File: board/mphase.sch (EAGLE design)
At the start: 4 parts, among them IC1 MAX232, IC2 PIC18F4455_40, X1 332-10, X2 332-10

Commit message: updates
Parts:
- added C1, C2, C3, C4, C5, C6, C7: (no value), resistor:C-US025-025X050
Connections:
- new net N$1: C1.2, IC1G$1.C1-
- new net N$10: IC1G$1.T2IN, IC2.TX2
- new net N$11: IC1G$1.T1IN, IC2.TX1
- new net N$12: IC1G$1.R1OUT, IC2.RX1
- new net N$13: IC1G$1.R2OUT, IC2.RX2
- new net N$2: C2.2, IC1G$1.C2-
- new net N$3: C2.1, IC1G$1.C2+
- new net N$4: C1.1, IC1G$1.C1+
- new net N$5: C3.2, IC1G$1.V+
- new net N$6: C4.1, IC1G$1.V-
- new net N$9: C5.1, IC2.VDDCORE
- new net VDD: C6.1, C7.1, IC2.VDD, IC2.VDD@1
- new net VSS: C3.1, C4.2, C7.2, IC2.VSS, IC2.VSS@1
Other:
- moved on the sheet: IC1, IC2
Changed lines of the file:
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@@
 <layer number="97" name="Info" color="7" fill="1" visible="yes" active="yes"/>
 <layer number="98" name="Guide" color="6" fill="1" visible="yes" active="yes"/>
+<layer number="99" name="SpiceOrder" color="5" fill="1" visible="yes" active="yes"/>
 </layers>
 <schematic xreflabel="%F%N/%S.%C%R" xrefpart="/%S.%C%R">
@@
 <part name="X2" library="con-garry" deviceset="332-10" device=""/>
 <part name="IC2" library="microchip" deviceset="PIC18F4*_40" device="" technology="455"/>
+<part name="C1" library="resistor" deviceset="C-US" device="025-025X050"/>
+<part name="C2" library="resistor" deviceset="C-US" device="025-025X050"/>
+<part name="C3" library="resistor" deviceset="C-US" device="025-025X050"/>
+<part name="C4" library="resistor" deviceset="C-US" device="025-025X050"/>
+<part name="C5" library="resistor" deviceset="C-US" device="025-025X050"/>
+<part name="C6" library="resistor" deviceset="C-US" device="025-025X050"/>
+<part name="C7" library="resistor" deviceset="C-US" device="025-025X050"/>
+<part name="VDD1" library="supply1" deviceset="VDD" device=""/>
+<part name="VDD2" library="supply1" deviceset="VDD" device=""/>
+<part name="VSS1" library="supply1" deviceset="VSS" device=""/>
+<part name="VSS2" library="supply1" deviceset="VSS" device=""/>
+<part name="VSS3" library="supply1" deviceset="VSS" device=""/>
+<part name="VSS4" library="supply1" deviceset="VSS" device=""/>
+<part name="VSS5" library="supply1" deviceset="VSS" device=""/>
+<part name="VSS6" library="supply1" deviceset="VSS" device=""/>
+<part name="VSS7" library="supply1" deviceset="VSS" device=""/>
 </parts>
 <sheets>
@@
 </plain>
 <instances>
-<instance part="IC1" gate="G$1" x="33.02" y="43.18"/>
+<instance part="IC1" gate="G$1" x="152.4" y="48.26"/>
 <instance part="X1" gate="-1" x="25.4" y="99.06"/>
 <instance part="X1" gate="-2" x="45.72" y="99.06"/>
@@
 <instance part="X2" gate="-9" x="91.44" y="88.9"/>
 <instance part="X2" gate="-10" x="111.76" y="88.9"/>
-<instance part="IC2" gate="G$1" x="93.98" y="45.72"/>
+<instance part="IC2" gate="G$1" x="40.64" y="45.72"/>
+<instance part="C1" gate="G$1" x="129.54" y="60.96"/>
+<instance part="C2" gate="G$1" x="129.54" y="50.8"/>
+<instance part="C3" gate="G$1" x="172.72" y="63.5"/>
+<instance part="C4" gate="G$1" x="177.8" y="50.8"/>
+<instance part="C5" gate="G$1" x="-10.16" y="58.42" rot="R270"/>
+<instance part="C6" gate="G$1" x="-10.16" y="45.72" rot="R270"/>
+<instance part="C7" gate="G$1" x="86.36" y="50.8" rot="R90"/>
+<instance part="VDD1" gate="G$1" x="-5.08" y="48.26"/>
+<instance part="VDD2" gate="G$1" x="83.82" y="53.34"/>
+<instance part="VSS1" gate="G$1" x="78.74" y="48.26" rot="R90"/>
+<instance part="VSS2" gate="G$1" x="177.8" y="43.18"/>
+<instance part="VSS3" gate="G$1" x="172.72" y="68.58" rot="R180"/>
+<instance part="VSS4" gate="G$1" x="93.98" y="50.8" rot="R90"/>
+<instance part="VSS5" gate="G$1" x="-15.24" y="45.72" rot="R270"/>
+<instance part="VSS6" gate="G$1" x="-15.24" y="58.42" rot="R270"/>
+<instance part="VSS7" gate="G$1" x="2.54" y="43.18" rot="R270"/>
 </instances>
 <busses>
 </busses>
 <nets>
+<net name="N$1" class="0">
+<segment>
+<pinref part="C1" gate="G$1" pin="2"/>
+<pinref part="IC1" gate="G$1" pin="C1-"/>
+<wire x1="129.54" y1="55.88" x2="137.16" y2="55.88" width="0.1524" layer="91"/>
+</segment>
+</net>
+<net name="N$2" class="0">
+<segment>
+<pinref part="C2" gate="G$1" pin="2"/>
+<pinref part="IC1" gate="G$1" pin="C2-"/>
+<wire x1="129.54" y1="45.72" x2="137.16" y2="45.72" width="0.1524" layer="91"/>
+</segment>
+</net>
+<net name="N$3" class="0">
+<segment>
+<pinref part="C2" gate="G$1" pin="1"/>
+<wire x1="129.54" y1="53.34" x2="137.16" y2="53.34" width="0.1524" layer="91"/>
+<pinref part="IC1" gate="G$1" pin="C2+"/>
+<wire x1="137.16" y1="53.34" x2="137.16" y2="50.8" width="0.1524" layer="91"/>
+</segment>
+</net>
+<net name="N$4" class="0">
+<segment>
+<pinref part="C1" gate="G$1" pin="1"/>
+<wire x1="129.54" y1="63.5" x2="137.16" y2="63.5" width="0.1524" layer="91"/>
+<pinref part="IC1" gate="G$1" pin="C1+"/>
+<wire x1="137.16" y1="63.5" x2="137.16" y2="60.96" width="0.1524" layer="91"/>
+</segment>
+</net>
+<net name="N$5" class="0">
+<segment>
+<pinref part="IC1" gate="G$1" pin="V+"/>
+<pinref part="C3" gate="G$1" pin="2"/>
+<wire x1="167.64" y1="58.42" x2="172.72" y2="58.42" width="0.1524" layer="91"/>
+</segment>
+</net>
+<net name="N$6" class="0">
+<segment>
+<pinref part="IC1" gate="G$1" pin="V-"/>
+<pinref part="C4" gate="G$1" pin="1"/>
+<wire x1="167.64" y1="53.34" x2="177.8" y2="53.34" width="0.1524" layer="91"/>
+</segment>
+</net>
+<net name="N$9" class="0">
+<segment>
+<pinref part="IC2" gate="G$1" pin="VDDCORE"/>
+<pinref part="C5" gate="G$1" pin="1"/>
+<wire x1="5.08" y1="58.42" x2="-7.62" y2="58.42" width="0.1524" layer="91"/>
+</segment>
+</net>
+<net name="N$10" class="0">
+<segment>
+<pinref part="IC2" gate="G$1" pin="TX2"/>
+<wire x1="76.2" y1="43.18" x2="104.14" y2="43.18" width="0.1524" layer="91"/>
+<wire x1="104.14" y1="43.18" x2="104.14" y2="38.1" width="0.1524" layer="91"/>
+<pinref part="IC1" gate="G$1" pin="T2IN"/>
+<wire x1="104.14" y1="38.1" x2="137.16" y2="38.1" width="0.1524" layer="91"/>
+</segment>
+</net>
+<net name="N$11" class="0">
+<segment>
+<pinref part="IC2" gate="G$1" pin="TX1"/>
+<wire x1="76.2" y1="33.02" x2="106.68" y2="33.02" width="0.1524" layer="91"/>
+<wire x1="106.68" y1="33.02" x2="106.68" y2="40.64" width="0.1524" layer="91"/>
+<pinref part="IC1" gate="G$1" pin="T1IN"/>
+<wire x1="106.68" y1="40.64" x2="137.16" y2="40.64" width="0.1524" layer="91"/>
+</segment>
+</net>
+<net name="N$12" class="0">
+<segment>
+<pinref part="IC2" gate="G$1" pin="RX1"/>
+<pinref part="IC1" gate="G$1" pin="R1OUT"/>
+<wire x1="76.2" y1="35.56" x2="137.16" y2="35.56" width="0.1524" layer="91"/>
+</segment>
+</net>
+<net name="N$13" class="0">
+<segment>
+<pinref part="IC2" gate="G$1" pin="RX2"/>
+<wire x1="76.2" y1="45.72" x2="109.22" y2="45.72" width="0.1524" layer="91"/>
+<wire x1="109.22" y1="45.72" x2="109.22" y2="33.02" width="0.1524" layer="91"/>
+<pinref part="IC1" gate="G$1" pin="R2OUT"/>
+<wire x1="109.22" y1="33.02" x2="137.16" y2="33.02" width="0.1524" layer="91"/>
+</segment>
+</net>
+<net name="VDD" class="0">
+<segment>
+<pinref part="C6" gate="G$1" pin="1"/>
+<pinref part="IC2" gate="G$1" pin="VDD"/>
+<wire x1="-7.62" y1="45.72" x2="-5.08" y2="45.72" width="0.1524" layer="91"/>
+<pinref part="VDD1" gate="G$1" pin="VDD"/>
+<wire x1="-5.08" y1="45.72" x2="5.08" y2="45.72" width="0.1524" layer="91"/>
+<junction x="-5.08" y="45.72"/>
+</segment>
+<segment>
+<pinref part="C7" gate="G$1" pin="1"/>
+<pinref part="IC2" gate="G$1" pin="VDD@1"/>
+<wire x1="83.82" y1="50.8" x2="76.2" y2="50.8" width="0.1524" layer="91"/>
+<pinref part="VDD2" gate="G$1" pin="VDD"/>
+<junction x="83.82" y="50.8"/>
+</segment>
+</net>
+<net name="VSS" class="0">
+<segment>
+<pinref part="C4" gate="G$1" pin="2"/>
+<pinref part="VSS2" gate="G$1" pin="VSS"/>
+</segment>
+<segment>
+<pinref part="C3" gate="G$1" pin="1"/>
+<pinref part="VSS3" gate="G$1" pin="VSS"/>
+</segment>
+<segment>
+<pinref part="C7" gate="G$1" pin="2"/>
+<pinref part="VSS4" gate="G$1" pin="VSS"/>
+</segment>
+<segment>
+<pinref part="IC2" gate="G$1" pin="VSS"/>
+<pinref part="VSS7" gate="G$1" pin="VSS"/>
+</segment>
+<segment>
+<pinref part="IC2" gate="G$1" pin="VSS@1"/>
+<pinref part="VSS1" gate="G$1" pin="VSS"/>
+</segment>
+</net>
 </nets>
 </sheet>

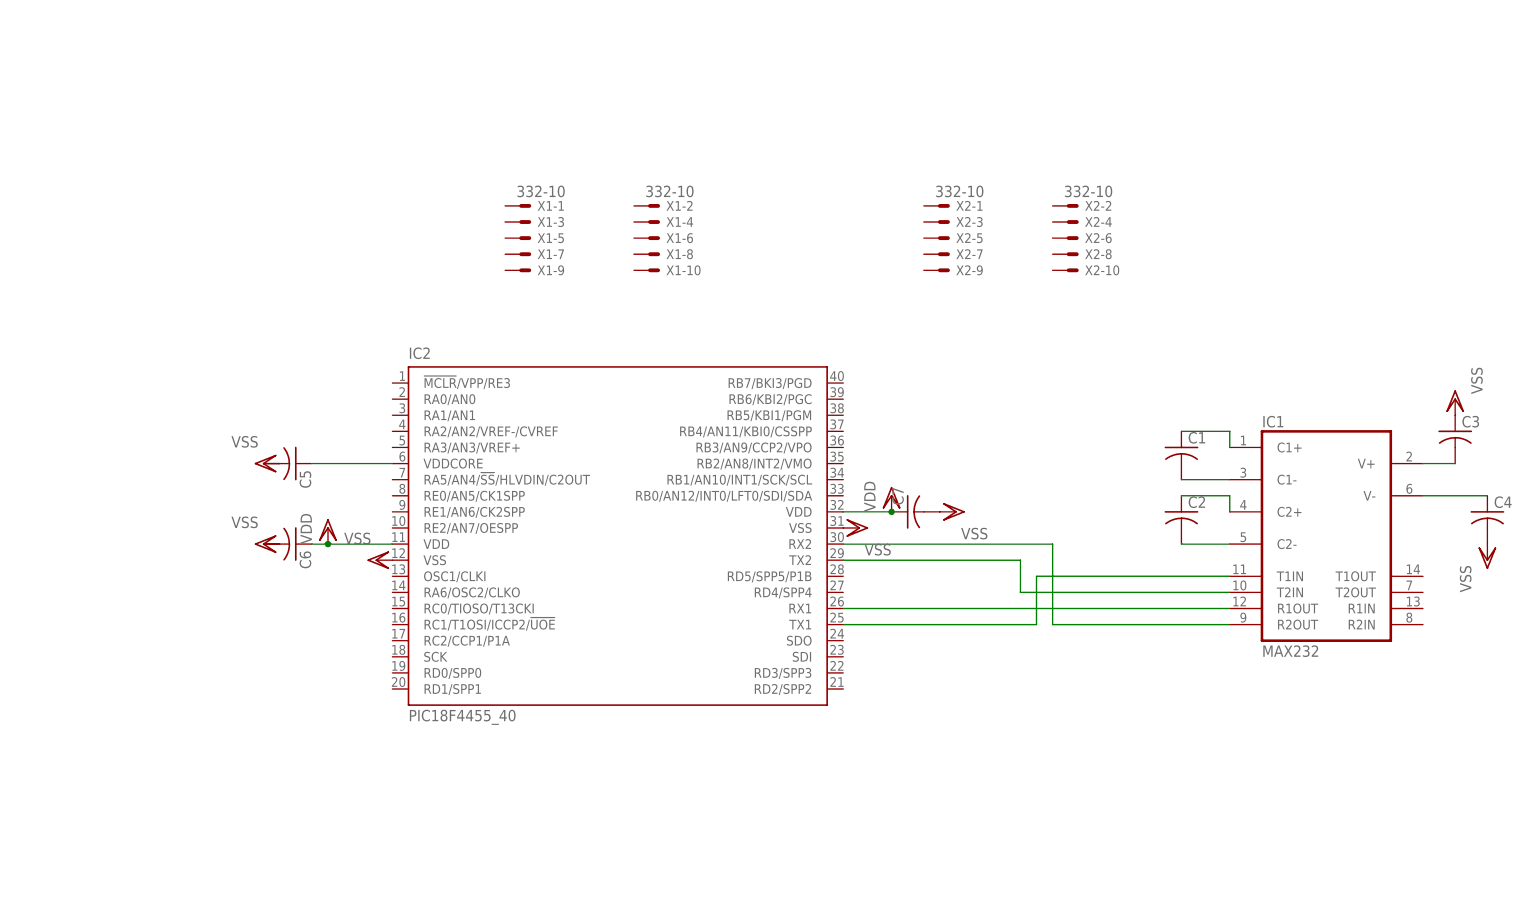
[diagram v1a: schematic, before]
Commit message: 
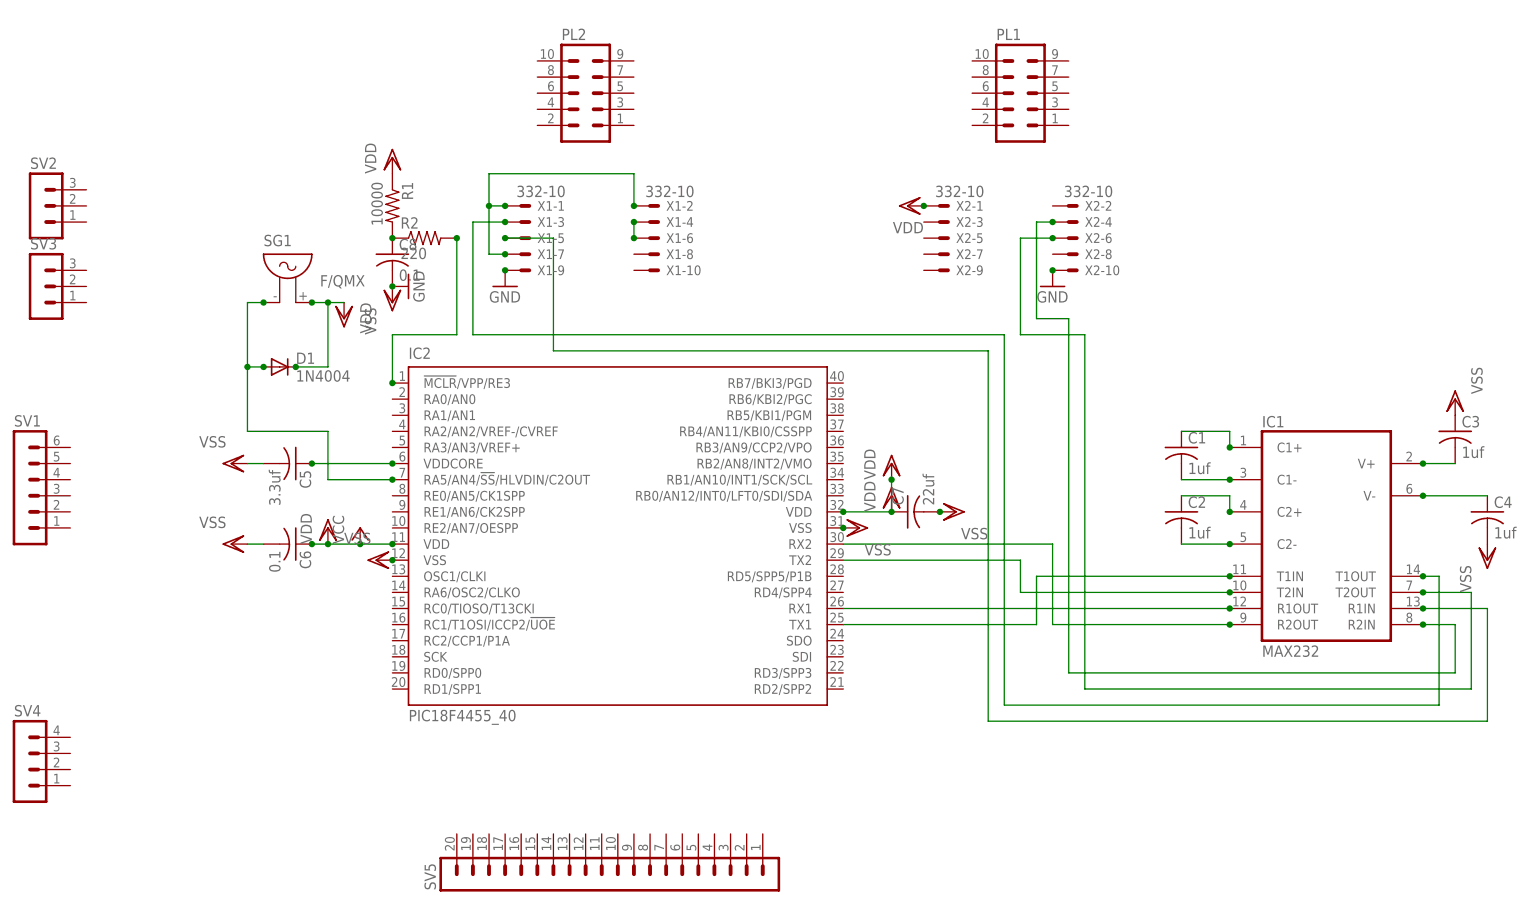
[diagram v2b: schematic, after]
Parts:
- added C8: 0.1, resistor:C-US025-024X044
- added D1: 1N4004, diode:1N4004
- added PL1, PL2: (no value), con-harting-h:10H
- added R1: 10000, resistor:R-US_0204/2V
- added R2: 220, resistor:R-US_0204/2V
- added SG1: F/QMX, buzzer:F/QMX
- added SV1: (no value), con-lstb:MA06-1
- added SV2, SV3: (no value), con-lstb:MA03-1
- added SV4: (no value), con-lstb:MA04-1
- added SV5: (no value), con-lstb:MA20-1
- C1, C2, C3, C4: value (none) -> 1uf
- C5: value (none) -> 3.3uf
- C6: value (none) -> 0.1
- C7: value (none) -> 22uf
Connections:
- new net GND: C8.2, X1-9.S, X2-10.S
- new net N$14: IC2.!MCLR!/VPP/RE3, R2.2
- new net N$15: IC1G$1.R2IN, X2-4.S
- new net N$16: IC1G$1.T2OUT, X2-6.S
- new net N$17: X1-4.S, X1-6.S
- new net N$18: X1-1.S, X1-2.S, X1-7.S
- new net N$19: IC1G$1.T1OUT, X1-3.S
- new net N$20: IC1G$1.R1IN, X1-5.S
- new net N$7: D1.A, IC2.RA5/AN4/!SS!/HLVDIN/C2OUT, SG1.1
- new net N$8: C8.1, R1.2, R2.1
- new net VCC: C6.1, IC2.VDD
- net VDD: now also D1.C, R1.1, SG1.2, X2-1.S; no longer C6.1, IC2.VDD
- net VSS: now also C5.2, C6.2

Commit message: update code
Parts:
- added C10, C9: 0.1, resistor:C-US025-024X044
- added C11: 22uf, resistor:C-US025-025X050
- added D2: BZX55, diode:BZX55
- added R4, R7: 10000, resistor:R-US_0204/2V
- added R5, R6: 220, resistor:R-US_0204/2V
- renumbered R2 to R3
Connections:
- removed net N$15: IC1G$1.R2IN, X2-4.S
- removed net N$18: X1-1.S, X1-2.S, X1-7.S
- new net N$21: C9.1, IC2.RB1/AN10/INT1/SCK/SCL, R4.2, R6.1
- new net N$22: C10.1, IC2.RB0/AN12/INT0/LFT0/SDI/SDA, R5.2, R7.1
- new net N$24: R6.2, SV2.2
- new net N$25: R5.1, SV2.3
- net GND: now also PL1.10, PL2.9
- net N$16: now also PL1.6
- net N$17: now also IC1G$1.R2IN, PL1.4, X2-4.S; no longer X1-4.S, X1-6.S
- net N$19: now also PL2.3
- net N$20: now also PL2.5
- net VDD: now also C11.1, D2.C, PL1.1, R4.1, R7.2, SV4.3
- net VSS: now also C10.2, C11.2, C9.2, D2.A, SV2.1, SV3.1, SV4.1
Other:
- moved on the sheet: C6, C7, C8, D1, R1, SG1, SV2, SV3

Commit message: update code
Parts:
- IC2: MPN (none) -> PIC18F45K80
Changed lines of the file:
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@@
 <grid distance="0.1" unitdist="inch" unit="inch" style="lines" multiple="1" display="no" altdistance="0.01" altunitdist="inch" altunit="inch"/>
 <layers>
-<layer number="1" name="Top" color="4" fill="1" visible="no" active="no"/>
-<layer number="2" name="Route2" color="1" fill="3" visible="no" active="no"/>
-<layer number="3" name="Route3" color="4" fill="3" visible="no" active="no"/>
-<layer number="14" name="Route14" color="1" fill="6" visible="no" active="no"/>
-<layer number="15" name="Route15" color="4" fill="6" visible="no" active="no"/>
-<layer number="16" name="Bottom" color="1" fill="1" visible="no" active="no"/>
-<layer number="17" name="Pads" color="2" fill="1" visible="no" active="no"/>
-<layer number="18" name="Vias" color="2" fill="1" visible="no" active="no"/>
-<layer number="19" name="Unrouted" color="6" fill="1" visible="no" active="no"/>
-<layer number="20" name="Dimension" color="15" fill="1" visible="no" active="no"/>
-<layer number="21" name="tPlace" color="7" fill="1" visible="no" active="no"/>
-<layer number="22" name="bPlace" color="7" fill="1" visible="no" active="no"/>
-<layer number="23" name="tOrigins" color="15" fill="1" visible="no" active="no"/>
-<layer number="24" name="bOrigins" color="15" fill="1" visible="no" active="no"/>
-<layer number="25" name="tNames" color="7" fill="1" visible="no" active="no"/>
-<layer number="26" name="bNames" color="7" fill="1" visible="no" active="no"/>
-<layer number="27" name="tValues" color="7" fill="1" visible="no" active="no"/>
-<layer number="28" name="bValues" color="7" fill="1" visible="no" active="no"/>
+<layer number="1" name="Top" color="4" fill="1" visible="yes" active="no"/>
+<layer number="2" name="Route2" color="1" fill="3" visible="yes" active="no"/>
+<layer number="3" name="Route3" color="4" fill="3" visible="yes" active="no"/>
+<layer number="14" name="Route14" color="1" fill="6" visible="yes" active="no"/>
+<layer number="15" name="Route15" color="4" fill="6" visible="yes" active="no"/>
+<layer number="16" name="Bottom" color="1" fill="1" visible="yes" active="no"/>
+<layer number="17" name="Pads" color="2" fill="1" visible="yes" active="no"/>
+<layer number="18" name="Vias" color="2" fill="1" visible="yes" active="no"/>
+<layer number="19" name="Unrouted" color="6" fill="1" visible="yes" active="no"/>
+<layer number="20" name="Dimension" color="15" fill="1" visible="yes" active="no"/>
+<layer number="21" name="tPlace" color="7" fill="1" visible="yes" active="no"/>
+<layer number="22" name="bPlace" color="7" fill="1" visible="yes" active="no"/>
+<layer number="23" name="tOrigins" color="15" fill="1" visible="yes" active="no"/>
+<layer number="24" name="bOrigins" color="15" fill="1" visible="yes" active="no"/>
+<layer number="25" name="tNames" color="7" fill="1" visible="yes" active="no"/>
+<layer number="26" name="bNames" color="7" fill="1" visible="yes" active="no"/>
+<layer number="27" name="tValues" color="7" fill="1" visible="yes" active="no"/>
+<layer number="28" name="bValues" color="7" fill="1" visible="yes" active="no"/>
 <layer number="29" name="tStop" color="7" fill="3" visible="no" active="no"/>
 <layer number="30" name="bStop" color="7" fill="6" visible="no" active="no"/>
@@
 <layer number="35" name="tGlue" color="7" fill="4" visible="no" active="no"/>
 <layer number="36" name="bGlue" color="7" fill="5" visible="no" active="no"/>
-<layer number="37" name="tTest" color="7" fill="1" visible="no" active="no"/>
-<layer number="38" name="bTest" color="7" fill="1" visible="no" active="no"/>
+<layer number="37" name="tTest" color="7" fill="1" visible="yes" active="no"/>
+<layer number="38" name="bTest" color="7" fill="1" visible="yes" active="no"/>
 <layer number="39" name="tKeepout" color="4" fill="11" visible="no" active="no"/>
 <layer number="40" name="bKeepout" color="1" fill="11" visible="no" active="no"/>
@@
 <layer number="44" name="Drills" color="7" fill="1" visible="no" active="no"/>
 <layer number="45" name="Holes" color="7" fill="1" visible="no" active="no"/>
-<layer number="46" name="Milling" color="3" fill="1" visible="no" active="no"/>
-<layer number="47" name="Measures" color="7" fill="1" visible="no" active="no"/>
-<layer number="48" name="Document" color="7" fill="1" visible="no" active="no"/>
-<layer number="49" name="Reference" color="7" fill="1" visible="no" active="no"/>
-<layer number="51" name="tDocu" color="7" fill="1" visible="no" active="no"/>
-<layer number="52" name="bDocu" color="7" fill="1" visible="no" active="no"/>
+<layer number="46" name="Milling" color="3" fill="1" visible="yes" active="no"/>
+<layer number="47" name="Measures" color="7" fill="1" visible="yes" active="no"/>
+<layer number="48" name="Document" color="7" fill="1" visible="yes" active="no"/>
+<layer number="49" name="Reference" color="7" fill="1" visible="yes" active="no"/>
+<layer number="51" name="tDocu" color="7" fill="1" visible="yes" active="no"/>
+<layer number="52" name="bDocu" color="7" fill="1" visible="yes" active="no"/>
 <layer number="90" name="Modules" color="5" fill="1" visible="yes" active="yes"/>
 <layer number="91" name="Nets" color="2" fill="1" visible="yes" active="yes"/>
@@
 <part name="X1" library="con-garry" deviceset="332-10" device=""/>
 <part name="X2" library="con-garry" deviceset="332-10" device=""/>
-<part name="IC2" library="microchip" deviceset="PIC18F4*_40" device="" technology="455"/>
+<part name="IC2" library="microchip" deviceset="PIC18F4*_40" device="" technology="455">
+<attribute name="MPN" value="PIC18F45K80"/>
+</part>
 <part name="C1" library="resistor" deviceset="C-US" device="025-025X050" value="1uf"/>
 <part name="C2" library="resistor" deviceset="C-US" device="025-025X050" value="1uf"/>
